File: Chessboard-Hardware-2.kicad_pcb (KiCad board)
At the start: 2 copper layers, 200 x 200 mm, 13 parts, among them J1 Conn_01x04_Pin, J2 Raspberry_Pi_0

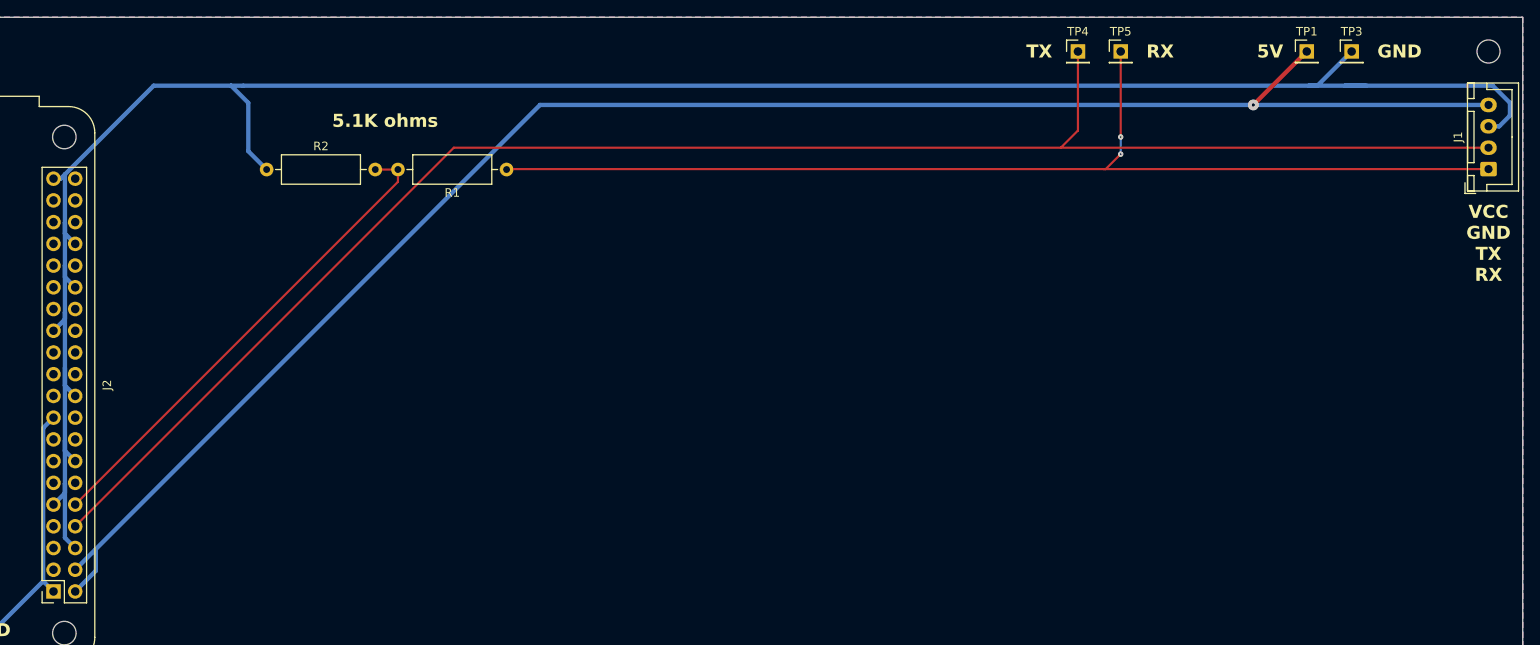
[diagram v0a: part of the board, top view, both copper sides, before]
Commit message: Shift serial JST-XH connector over for space
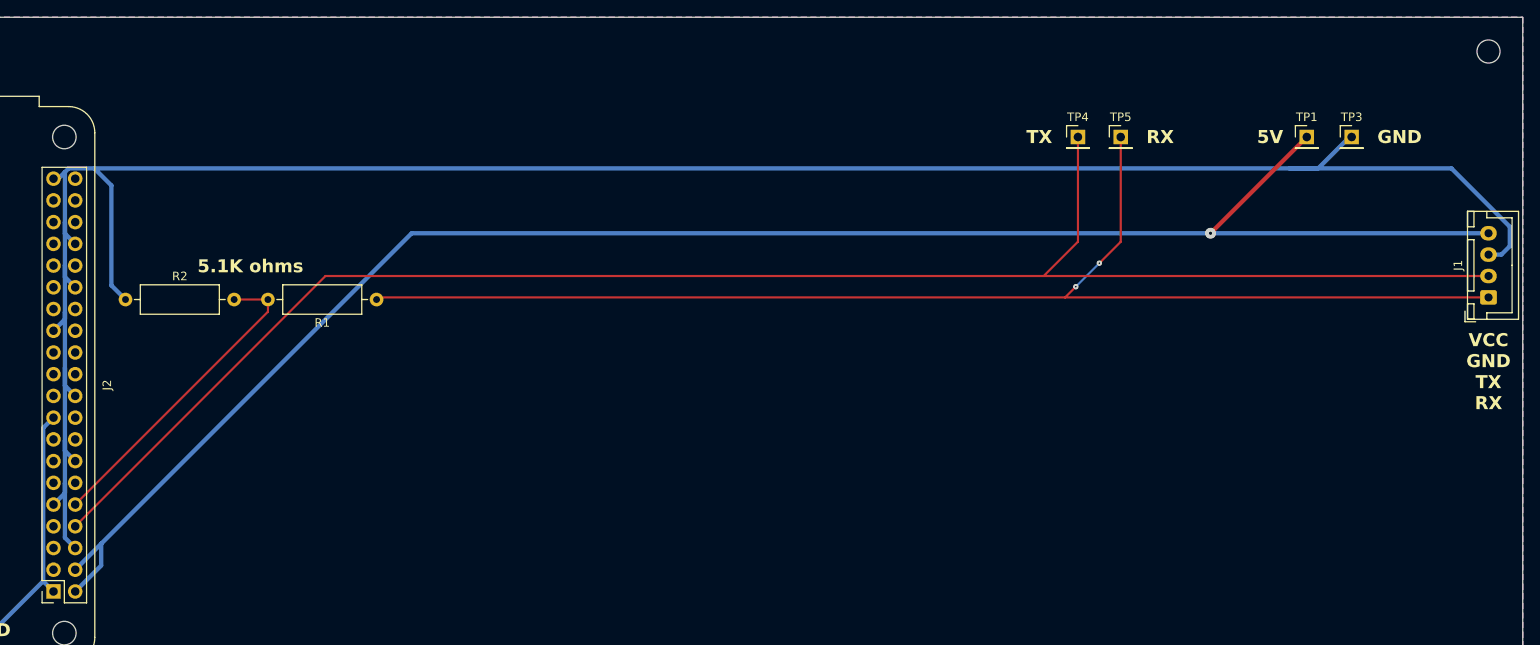
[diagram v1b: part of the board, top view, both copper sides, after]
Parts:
- moved R2 22.4 mm to (86.7, 83.0)
- moved R1 21.5 mm to (116.0, 83.0)
- moved J1 15.0 mm to (246.0, 82.8)
- moved TP1 10.0 mm to (224.8, 64.0)
- moved TP3 10.0 mm to (230.0, 64.0)
- moved TP4 10.0 mm to (198.0, 64.0)
- moved TP5 10.0 mm to (203.0, 64.0)
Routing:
- net Net-(J1-Pin_1): track 129.5 -> 151.5 mm
- net /RX: track 57.4 -> 37.3 mm
- net GND: track 263.4 -> 267.3 mm
- net +5V: track 202.5 -> 204.3 mm
